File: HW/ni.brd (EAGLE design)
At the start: 122.5 x 35 mm, 71 parts, among them IC1 FAN3100TSX, IC2 STM32G071CBU6, IC3 MIC5504-3.3YM5-TR, Q1 FQD12N20L, Q10 CPH3461, Q11 CPH3461, Q12 CPH3461, Q13 BF821SMD, Q14 CPH3461, Q15 BF821SMD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

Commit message: HW_values added
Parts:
- C3, C8: value (none) -> 4.3p
- R16: value (none) -> 15k
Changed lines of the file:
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@@
 <attribute name="VALUE" x="51.875" y="5.625" size="1.27" layer="27" rot="R135" align="center"/>
 </element>
-<element name="C3" library="rcl" library_urn="urn:adsk.eagle:library:334" package="C0402" package3d_urn="urn:adsk.eagle:package:23626/2" value="" x="57.5" y="-0.625" smashed="yes">
+<element name="C3" library="rcl" library_urn="urn:adsk.eagle:library:334" package="C0402" package3d_urn="urn:adsk.eagle:package:23626/2" value="4.3p" x="57.5" y="-0.625" smashed="yes">
 <attribute name="NAME" x="59.365" y="-1.864996875" size="1.016" layer="25" font="vector" ratio="10"/>
 <attribute name="POPULARITY" value="18" x="57.5" y="-0.625" size="1.778" layer="27" display="off"/>
@@
 <attribute name="VALUE" x="53.721" y="-2.521" size="1.27" layer="27"/>
 </element>
-<element name="C8" library="rcl" library_urn="urn:adsk.eagle:library:334" package="C0402" package3d_urn="urn:adsk.eagle:package:23626/2" value="" x="52.002" y="-0.625" smashed="yes">
+<element name="C8" library="rcl" library_urn="urn:adsk.eagle:library:334" package="C0402" package3d_urn="urn:adsk.eagle:package:23626/2" value="4.3p" x="52.002" y="-0.625" smashed="yes">
 <attribute name="NAME" x="48.867" y="-1.865" size="1.016" layer="25" font="vector" ratio="10"/>
 <attribute name="POPULARITY" value="18" x="52.002" y="-0.625" size="1.778" layer="27" display="off"/>
@@
 <attribute name="VALUE" x="67.453" y="11.654" size="1.27" layer="27" rot="R90"/>
 </element>
-<element name="R16" library="rcl" library_urn="urn:adsk.eagle:library:334" package="R0402" package3d_urn="urn:adsk.eagle:package:23547/3" value="" x="64.973" y="9.802" smashed="yes" rot="R180">
+<element name="R16" library="rcl" library_urn="urn:adsk.eagle:library:334" package="R0402" package3d_urn="urn:adsk.eagle:package:23547/3" value="15k" x="64.973" y="9.802" smashed="yes" rot="R180">
 <attribute name="NAME" x="66.233" y="9.294" size="1.016" layer="25" font="vector" ratio="10" rot="R180"/>
 <attribute name="POPULARITY" value="0" x="64.973" y="9.802" size="1.778" layer="27" rot="R180" display="off"/>

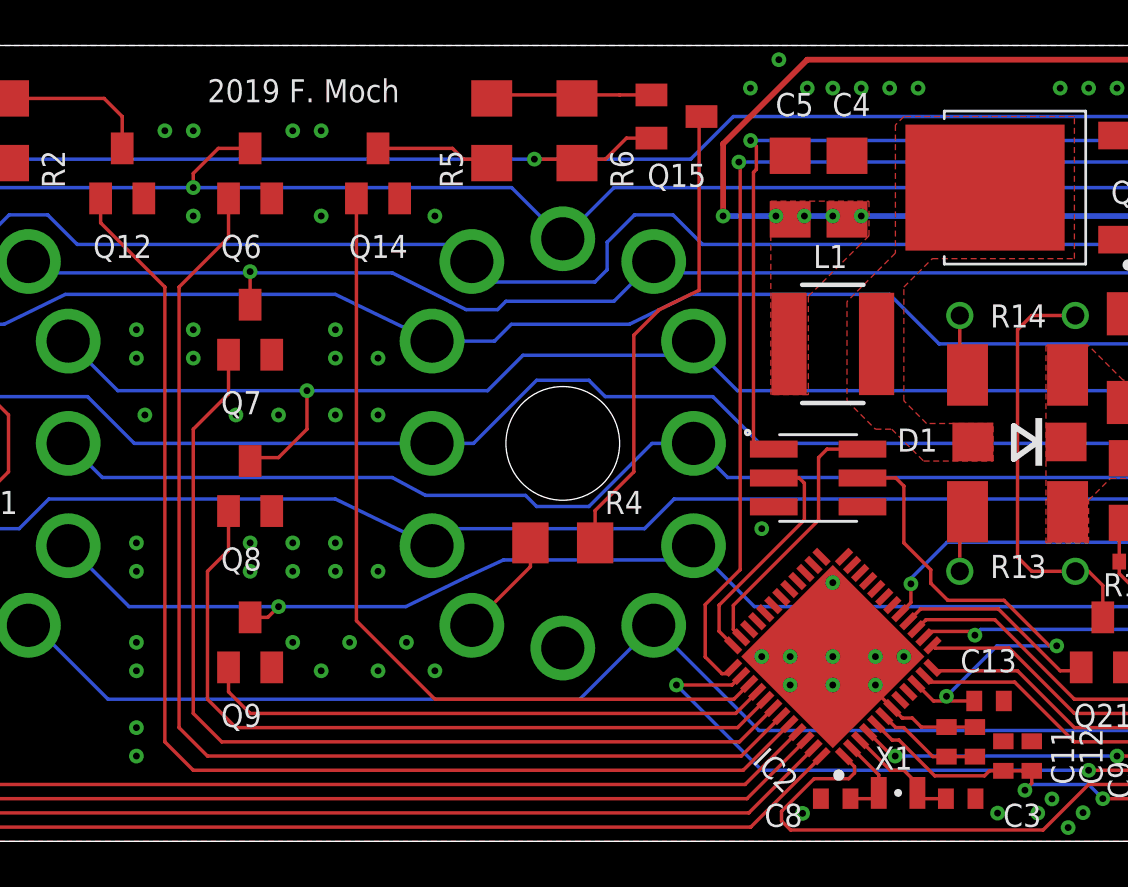
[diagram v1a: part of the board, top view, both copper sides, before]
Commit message: HW V1.1 fixed 3.3V supply
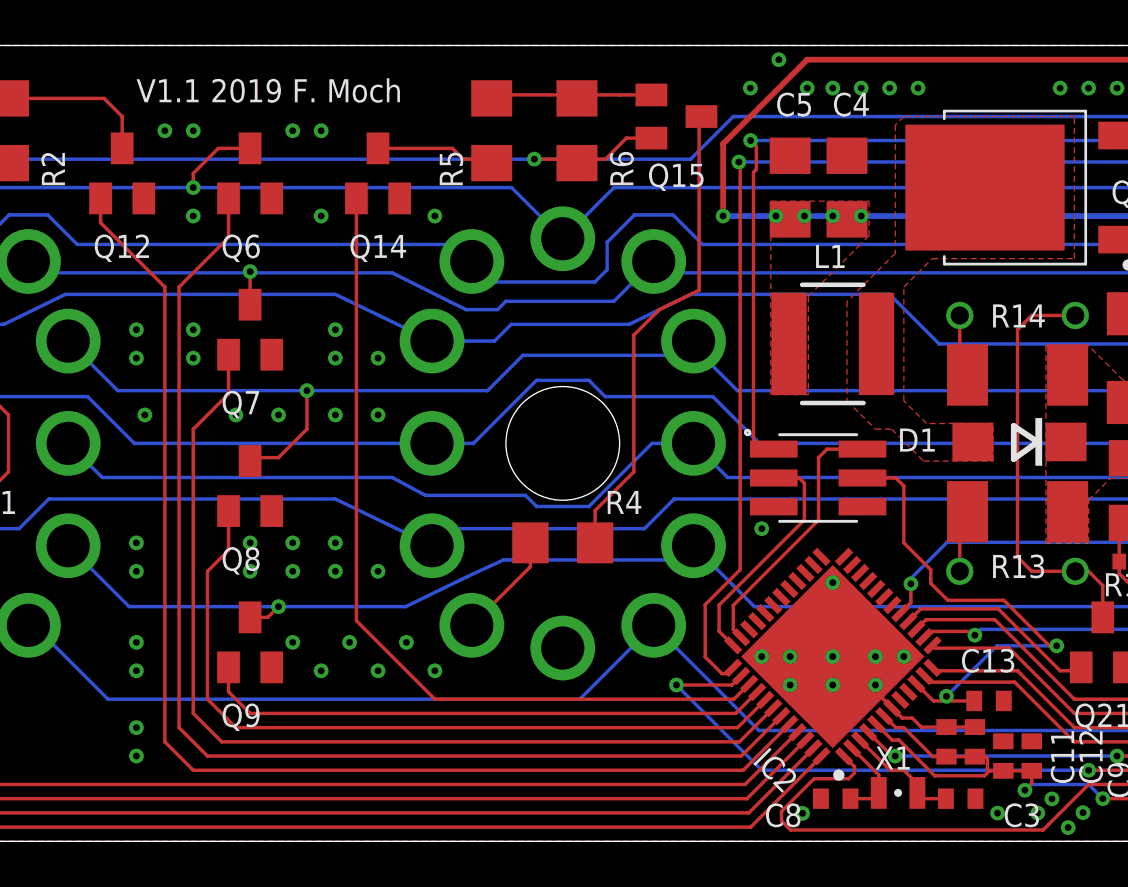
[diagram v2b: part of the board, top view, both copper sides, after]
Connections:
- removed net N$18: C11.1, C12.1, IC2.6
- net +3V3: now also C11.1, C12.1, IC2.6
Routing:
- net +3V3: track 168.8 -> 174.7 mm
- net N$18: track 4.73 -> 0.00 mm
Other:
- board text added: "V1.1 2019 F. Moch"
- board text removed: "2019 F. Moch"
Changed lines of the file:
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@@
 <wire x1="119.25" y1="32.5" x2="0.75" y2="32.5" width="0" layer="20"/>
 <wire x1="0.75" y1="32.5" x2="-1.25" y2="30.5" width="0" layer="20" curve="90"/>
-<text x="24.375" y="30" size="1.016" layer="25" font="vector" ratio="10">2019 F. Moch</text>
+<text x="21.25" y="30" size="1.016" layer="25" font="vector" ratio="10">V1.1 2019 F. Moch</text>
 </plain>
 <attributes>
@@
 </pass>
 </autorouter>
+<groups>
+<board_group name="1"/>
+</groups>
 <elements>
 <element name="N4" library="Nixie" library_urn="urn:adsk.eagle:library:1509144" package="IN-12" package3d_urn="urn:adsk.eagle:package:1509184/3" value="IN-12-V3" x="12.5" y="15" smashed="yes" rot="MR0">
@@
 <wire x1="26.25" y1="3.125" x2="25.3" y2="4.075" width="0.1524" layer="1"/>
 </signal>
-<signal name="N$18">
-<contactref element="IC2" pad="6"/>
-<contactref element="C11" pad="1"/>
-<contactref element="C12" pad="1"/>
-<wire x1="54.137740625" y1="3.008703125" x2="54.64644375" y2="2.5" width="0.1524" layer="1"/>
-<wire x1="54.64644375" y1="2.5" x2="55" y2="2.5" width="0.1524" layer="1"/>
-<wire x1="56.275" y1="1.225" x2="56.875" y2="1.225" width="0.1524" layer="1"/>
-<wire x1="55" y1="2.5" x2="56.275" y2="1.225" width="0.1524" layer="1"/>
-<wire x1="56.875" y1="1.225" x2="58.125" y2="1.225" width="0.1524" layer="1"/>
-</signal>
 <signal name="N$19" class="1">
 <contactref element="N4" pad="12"/>
@@
 <wire x1="63.75" y1="-0.625" x2="93.75" y2="-0.625" width="0.1524" layer="1"/>
 <wire x1="93.75" y1="-0.625" x2="94.975" y2="0.6" width="0.1524" layer="1"/>
+<contactref element="IC2" pad="6"/>
+<contactref element="C11" pad="1"/>
+<contactref element="C12" pad="1"/>
+<wire x1="54.137740625" y1="3.008703125" x2="54.64644375" y2="2.5" width="0.1524" layer="1"/>
+<wire x1="54.64644375" y1="2.5" x2="55" y2="2.5" width="0.1524" layer="1"/>
+<wire x1="56.275" y1="1.225" x2="56.875" y2="1.225" width="0.1524" layer="1"/>
+<wire x1="55" y1="2.5" x2="56.275" y2="1.225" width="0.1524" layer="1"/>
+<wire x1="56.875" y1="1.225" x2="58.125" y2="1.225" width="0.1524" layer="1"/>
+<wire x1="58.766" y1="0.6" x2="58.674" y2="0.692" width="0.1524" layer="1"/>
+<wire x1="58.674" y1="0.692" x2="58.674" y2="1.143" width="0.1524" layer="1"/>
+<wire x1="58.674" y1="1.143" x2="58.592" y2="1.225" width="0.1524" layer="1"/>
+<wire x1="58.592" y1="1.225" x2="58.125" y2="1.225" width="0.1524" layer="1"/>
 </signal>
 <signal name="N$17" class="1">
@@
 packages will not be understood (or retained) with this version.
 </note>
+<note version="9.5" severity="warning">
+Since Version 9.5, EAGLE supports persistent groups with
+schematics, and board files. Those persistent groups
+will not be understood (or retained) with this version.
+</note>
 <note version="9.4" severity="warning">

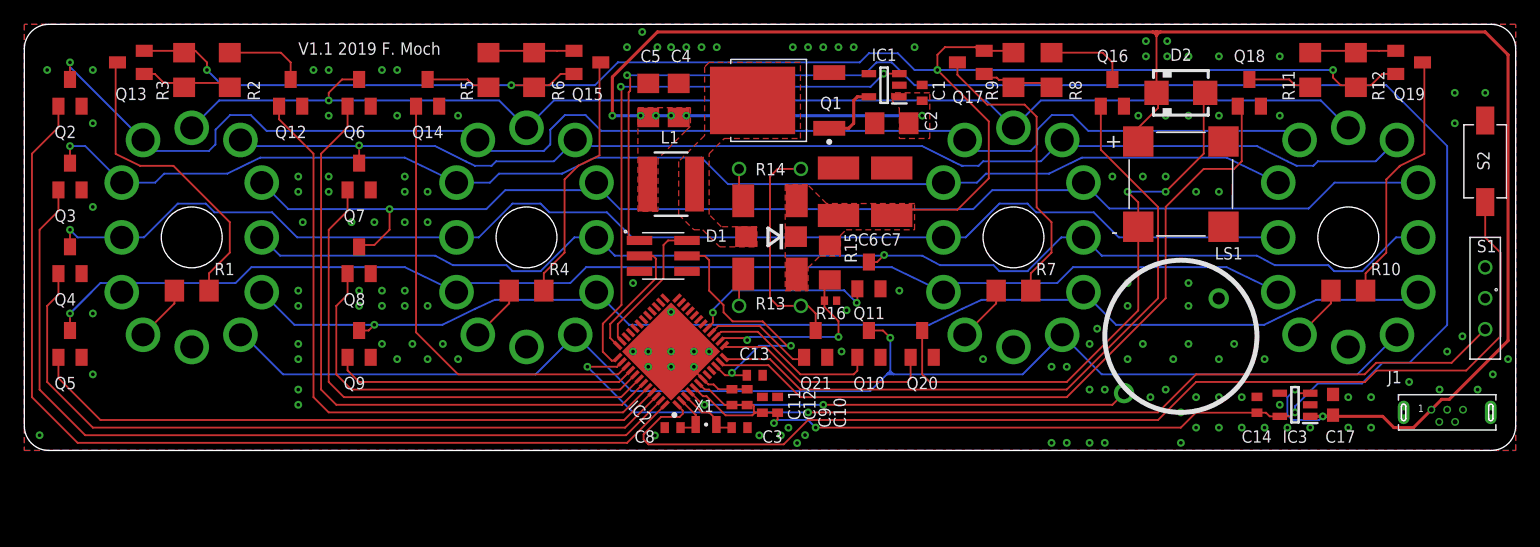
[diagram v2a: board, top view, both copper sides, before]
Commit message: V1.1 fixed nixie footprint
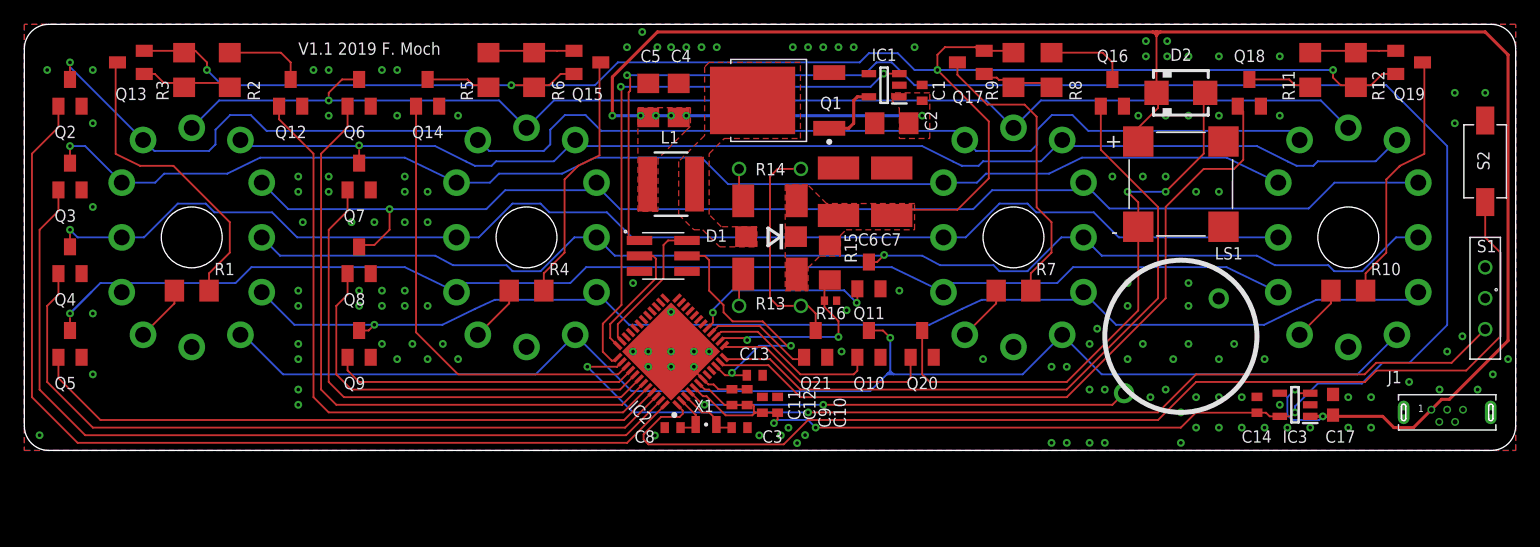
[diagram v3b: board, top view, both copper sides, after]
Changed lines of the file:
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@@
 <attribute name="VALUE" x="13.77" y="8.65" size="0.8128" layer="28" rot="MR0"/>
 </element>
-<element name="N3" library="Nixie" library_urn="urn:adsk.eagle:library:1509144" package="IN-12" package3d_urn="urn:adsk.eagle:package:1509184/3" override_package3d_urn="urn:adsk.eagle:package:1509184/9" override_package_urn="urn:adsk.eagle:footprint:1509183/5" value="IN-12-V3" x="40" y="15" smashed="yes" rot="MR0">
+<element name="N3" library="Nixie" library_urn="urn:adsk.eagle:library:1509144" package="IN-12" package3d_urn="urn:adsk.eagle:package:1509184/3" override_package3d_urn="urn:adsk.eagle:package:1509184/9" override_package_urn="urn:adsk.eagle:footprint:1509183/5" override_locally_modified="yes" value="IN-12-V3" x="40" y="15" smashed="yes" rot="MR0">
 <attribute name="NAME" x="41.29" y="9.305" size="1.27" layer="26" rot="MR0"/>
 <attribute name="VALUE" x="41.27" y="8.65" size="0.8128" layer="28" rot="MR0"/>
@@
 <attribute name="VALUE" x="81.27" y="8.65" size="0.8128" layer="28" rot="MR0"/>
 </element>
-<element name="N1" library="Nixie" library_urn="urn:adsk.eagle:library:1509144" package="IN-12" package3d_urn="urn:adsk.eagle:package:1509184/3" override_package3d_urn="urn:adsk.eagle:package:1509184/6" override_package_urn="urn:adsk.eagle:footprint:1509183/3" value="IN-12-V3" x="107.5" y="15" smashed="yes" rot="MR0">
+<element name="N1" library="Nixie" library_urn="urn:adsk.eagle:library:1509144" package="IN-12" package3d_urn="urn:adsk.eagle:package:1509184/3" override_package3d_urn="urn:adsk.eagle:package:1509184/6" override_package_urn="urn:adsk.eagle:footprint:1509183/3" override_locally_modified="yes" value="IN-12-V3" x="107.5" y="15" smashed="yes" rot="MR0">
 <attribute name="NAME" x="108.79" y="9.305" size="1.27" layer="26" rot="MR0"/>
 <attribute name="VALUE" x="108.77" y="8.65" size="0.8128" layer="28" rot="MR0"/>
@@
 <wire x1="92.5" y1="17.5" x2="95.625" y2="20.625" width="0.1524" layer="1"/>
 <wire x1="95.625" y1="20.625" x2="98.125" y2="20.625" width="0.1524" layer="1"/>
-<wire x1="98.125" y1="20.625" x2="98.75" y2="21.25" width="0.1524" layer="1"/>
-<wire x1="98.75" y1="21.25" x2="98.75" y2="25.45" width="0.1524" layer="1"/>
-<wire x1="98.75" y1="25.45" x2="98.425" y2="25.775" width="0.1524" layer="1"/>
+<wire x1="98.125" y1="20.625" x2="98.877" y2="21.377" width="0.1524" layer="1"/>
+<wire x1="98.877" y1="21.377" x2="98.877" y2="25.323" width="0.1524" layer="1"/>
+<wire x1="98.877" y1="25.323" x2="98.425" y2="25.775" width="0.1524" layer="1"/>
 <wire x1="84.375" y1="1.875" x2="92.5" y2="10" width="0.1524" layer="1"/>
 </signal>

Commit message: Zwischenstand zu V1.1 Revision
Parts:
- added S3: (no value), Wurth_Elektronik_Electromechanic_Switch_rev18c:434121050816
- added SV1: (no value), con-lstb:MA03-1
- moved S1 5.65 mm to (116.1, 15.0)
- moved J1 3.75 mm to (111.9, 0.62)
- moved S2 0.88 mm to (119.4, 20.6)
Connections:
- removed net SWO: J3.4
- new net S3: IC2.9
- net +3V3: no longer J3.1
- net GND: now also S3.2
- net NRST: no longer J3.5
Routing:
- net +3V3: track 174.7 -> 58.1 mm, vias 4 -> 2
- net S3: track 0.00 -> 46.0 mm, vias 0 -> 3
- net S2: track 91.0 -> 66.8 mm
- net NRST: track 22.4 -> 2.99 mm, vias 2 -> 0
- net +5V: track 166.4 -> 147.7 mm
- net S1: track 81.1 -> 69.7 mm
- net G7: track 79.6 -> 81.1 mm
- net V+: track 143.0 -> 142.1 mm
- net GND: vias 144 -> 129
